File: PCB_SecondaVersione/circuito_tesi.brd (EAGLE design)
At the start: 100 x 80 mm, 52 parts, among them IC1 SCD41-D-R2, IC2 TPS60120PWPR, IC3 TPS78918DBVR, Q1 BSS138, Q2 BSS138, Q3 BSS138, Q4 BSS138, U1 TSV912IDT, U2 SGP30, U3 MICS-6814, U5 317030213, U6 BME280, U7 LIS3DH, U8 MAX682ESA+

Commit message: Sistemato circuito
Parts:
- removed C1, C12: CL05A106MP5NUNC, Condens_10uF:CAPC1005X55N
- removed C10, C11, C6: GRM033R60J105MEA2D, Condens_1uF:CAPC0603X35N
- removed C2, C3, C5: GRM033R61A225KE47D, Condens_2.2uF:CAPC0603X39N
- removed C4: CL05A226MQ5N6J8, Condens_22uF:CAPC1005X55N
- removed IC2: TPS60120PWPR, C_P_3.3_TPS60120PWPR:SOP65P640X120-21N
- removed IC3: TPS78918DBVR, V_REG_1.8_SOT-23-5:SOT95P280X145-5N
- removed R18: ERA6VEB8200V, Res_820_0p25W:RES_ERA6VEB8200V
- removed U8: MAX682ESA+, C_P_5_MAX682ESA_:SOIC127P600X175-8N
- added U10, U4, U9: LD1117S33TR, V_Reg_3.3_SMD:SOT230P700X180-4N
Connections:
- net N$15 renamed AIN3
- net N$17 renamed AIN1
- removed net 3.3: C13.1, C4.2, C5.2, IC2.16, Q3.1, Q4.1, R1.2, R11.2, R13.2, R14.2, R16.2, R18.2, R2.2, U5.11, U6.2, U6.6, U6.8, U7.1, U7.14, U7.8, U8.1, U8.3
- removed net N$14: C3.2, IC2.15
- removed net N$18: C3.1, IC2.13
- removed net N$19: IC2.4, IC2.5
- removed net N$20: C6.2, U8.6
- removed net N$22: C6.1, U8.7
- removed net N$23: Q1.2, R10.1, U2.6
- removed net N$24: R18.1, U8.2
- removed net N$7 (its old number): C2.2, IC2.6
- new net 3.3V: C13.1, IC1.19, IC1.7, Q3.1, Q4.1, R11.1, R13.2, R14.2, R16.1, U5.11, U6.2, U6.6, U6.8, U7.1, U7.14, U7.8, U9.2, U9.4
- new net N$25: BT3.-, BT4.S+1, BT4.S+2
- new net N$27: BT1.S+1, BT1.S+2, S2.2
- new net N$5: Q4.3, R17.1, SPS30.3
- new net SWDCLK: U5.36
- new net SWDIO: U5.37
- net 1.8V: now also R10.1, U10.2, U10.4; no longer C10.2, IC3.5, R10.2
- net 5V: now also U4.2, U4.4; no longer C12.1, IC1.19, IC1.7, U8.8
- net GND: now also U10.1, U4.1, U9.1; no longer BT3.-, C1.2, C10.1, C11.1, C12.2, C4.1, C5.1, IC2.1, IC2.10, IC2.11, IC2.12, IC2.19, IC2.2, IC2.20, IC2.9, IC3.2, U8.4, U8.5
- net N$1: no longer IC1.10
- net N$12: now also Q1.2, R10.2, U2.6; no longer C2.1, IC2.8
- net N$2: now also BT1.-; no longer BT1.S+1, BT1.S+2, S2.2
- net N$3: now also R1.1, R2.1; no longer IC1.9, Q4.3, R17.1, SPS30.3
- net N$4: no longer BT1.-, BT4.S+1, BT4.S+2
- net SCL: now also IC1.9, R1.2, R11.2, R16.2; no longer R11.1, R16.1, R2.1
- net SDA: now also IC1.10, R2.2; no longer R1.1
- net VDD: now also S2.1, U10.3, U4.3, U9.3; no longer C1.1, C11.2, IC2.14, IC2.3, IC2.7, IC3.1, IC3.3, S2.3
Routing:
- net 3.3: track 131.5 -> 0.00 mm, vias 6 -> 0
- net N$4: track 94.0 -> 0.00 mm
- net GND: track 77.9 -> 14.9 mm
- net 5V: track 60.9 -> 0.55 mm, vias 1 -> 0
- net N$2: track 60.0 -> 0.00 mm
- net SCL: track 58.6 -> 0.00 mm, vias 2 -> 0
- net SDA: track 64.2 -> 9.55 mm
- net 1.8V: track 45.5 -> 3.63 mm, vias 1 -> 0
- net 3.3V: track 0.00 -> 41.2 mm, vias 0 -> 1
- net VDD: track 40.0 -> 0.00 mm
- net N$23: track 10.3 -> 0.00 mm
- net N$3: track 8.36 -> 0.00 mm
- net AIN1: track 9.64 -> 2.09 mm
- net N$1: track 13.2 -> 9.63 mm
- net N$16: track 11.1 -> 7.86 mm
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
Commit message: Inizio PCB
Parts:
- moved C9 120.6 mm to (-81.3, 82.5), turned to 0 degrees
- moved LED2 117.3 mm to (-61.0, 14.0), turned to 0 degrees
- moved C7 114.7 mm to (-63.5, 82.5), turned to 0 degrees
- moved C8 110.9 mm to (-72.4, 82.5), turned to 0 degrees
- moved R1 110.1 mm to (-76.2, 72.4), turned to 0 degrees
- moved R17 101.2 mm to (-80.0, 78.7)
- moved R16 99.5 mm to (-72.4, 78.7)
- moved R9 99.0 mm to (-48.3, 82.5)
- moved C13 98.3 mm to (-54.6, 82.5), turned to 0 degrees
- moved U1 97.8 mm to (-73.7, 45.7)
- moved U6 94.6 mm to (-58.4, 72.4), turned to 0 degrees
- moved R8 88.1 mm to (-67.3, 72.4), turned to 0 degrees
- moved U2 86.4 mm to (-38.1, 73.7), turned to 0 degrees
- moved R12 86.3 mm to (-41.9, 78.7)
- moved U7 85.7 mm to (-53.3, 72.4), turned to 0 degrees
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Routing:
- net 3.3V: track 41.2 -> 0.00 mm, vias 1 -> 0
- net N$6: track 16.1 -> 0.00 mm
- net GND: track 14.9 -> 0.00 mm
- net N$21: track 9.71 -> 0.00 mm
- net N$1: track 9.63 -> 0.00 mm
- net SDA: track 9.55 -> 0.00 mm
- net N$16: track 7.86 -> 0.00 mm
- net AIN3: track 7.43 -> 0.00 mm
- net N$11: track 6.97 -> 0.00 mm
- net N$12: track 4.79 -> 0.00 mm
- net N$8: track 4.13 -> 0.00 mm
- net 1.8V: track 3.63 -> 0.00 mm
- net N$10: track 3.56 -> 0.00 mm
- net N$9: track 2.90 -> 0.00 mm
- net N$13: track 2.21 -> 0.00 mm
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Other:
- outline, holes or cut-outs redrawn
- board text removed: "QUA CONNETTORI SPS30"

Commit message: Aggiunto SGP30
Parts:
- removed S2: JS102011SAQN, switch_JS102011SAQN:SW_JS102011SAQN
- added S1: EG1213, switch_TH_HO:SW_EG1213
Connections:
- net N$27: now also S1.2; no longer S2.2
- net VDD: now also S1.1; no longer S2.1
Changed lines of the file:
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@@
 <attribute name="VALUE" x="-49.7" y="81.75" size="0.5" layer="27" align="top-left"/>
-</element>
-<element name="S2" library="switch_JS102011SAQN" package="SW_JS102011SAQN" value="JS102011SAQN" x="49.55" y="47.34" smashed="yes" rot="MR270">
-<attribute name="DESCRIPTION" value=" Slide Switch SPDT Surface Mount, Right Angle " x="94" y="-6" size="1.778" layer="28" rot="MR270" display="off"/>
-<attribute name="DIGI-KEY_PART_NUMBER" value="401-1999-2-ND" x="94" y="-6" size="1.778" layer="28" rot="MR270" display="off"/>
-<attribute name="MF" value="C&amp;K" x="94" y="-6" size="1.778" layer="28" rot="MR270" display="off"/>
-<attribute name="MP" value="JS102011SAQN" x="94" y="-6" size="1.778" layer="28" rot="MR270" display="off"/>
-<attribute name="NAME" x="52.5522" y="52.14353125" size="1.27093125" layer="26" rot="MR0"/>
-<attribute name="PACKAGE" value="None" x="94" y="-6" size="1.778" layer="28" rot="MR270" display="off"/>
-<attribute name="PURCHASE-URL" value="https://pricing.snapeda.com/search/part/JS102011SAQN/?ref=eda" x="94" y="-6" size="1.778" layer="28" rot="MR270" display="off"/>
-<attribute name="VALUE" x="52.85288125" y="41.23466875" size="1.271109375" layer="28" rot="MR0"/>
 </element>
 <element name="SPS30" library="con-lstb" library_urn="urn:adsk.eagle:library:162" package="MA05-1" package3d_urn="urn:adsk.eagle:package:8332/1" value="" x="-74.93" y="60.96" smashed="yes">
@@
 <attribute name="PURCHASE-URL" value="https://pricing.snapeda.com/search/part/LD1117S33TR/?ref=eda" x="0" y="0" size="1.778" layer="27" display="off"/>
 <attribute name="VALUE" x="-52.071190625" y="58.3668" size="1.270590625" layer="27"/>
+</element>
+<element name="S1" library="switch_TH_HO" package="SW_EG1213" value="EG1213" x="48.7" y="46.9" smashed="yes" rot="MR270">
+<attribute name="DESCRIPTION" value=" Slide Switch SPDT Through Hole, Right Angle " x="48.7" y="46.9" size="1.778" layer="28" rot="MR270" display="off"/>
+<attribute name="DIGI-KEY_PART_NUMBER" value="EG1906-ND" x="48.7" y="46.9" size="1.778" layer="28" rot="MR270" display="off"/>
+<attribute name="MF" value="E-Switch" x="48.7" y="46.9" size="1.778" layer="28" rot="MR270" display="off"/>
+<attribute name="MP" value="EG1213" x="48.7" y="46.9" size="1.778" layer="28" rot="MR270" display="off"/>
+<attribute name="PACKAGE" value="None" x="48.7" y="46.9" size="1.778" layer="28" rot="MR270" display="off"/>
+<attribute name="PURCHASE-URL" value="https://pricing.snapeda.com/search/part/EG1213/?ref=eda" x="48.7" y="46.9" size="1.778" layer="28" rot="MR270" display="off"/>
 </element>
 </elements>
@@
 <contactref element="BT1" pad="S+1"/>
 <contactref element="BT1" pad="S+2"/>
-<contactref element="S2" pad="2"/>
-<wire x1="32.84" y1="36.65" x2="47.44" y2="36.65" width="0" layer="19" extent="1-1"/>
-<wire x1="46.8" y1="47.34" x2="32.84" y2="36.65" width="0" layer="19" extent="1-1"/>
+<contactref element="S1" pad="2"/>
+<wire x1="32.84" y1="36.65" x2="48.7" y2="46.9" width="0" layer="19" extent="16-16"/>
+<wire x1="47.44" y1="36.65" x2="32.84" y2="36.65" width="0" layer="19" extent="16-16"/>
 </signal>
 <signal name="VDD">
-<contactref element="S2" pad="1"/>
 <contactref element="U4" pad="3"/>
 <contactref element="U9" pad="3"/>
 <contactref element="U10" pad="3"/>
-<wire x1="-52.43" y1="61.2" x2="-38.46" y2="61.2" width="0" layer="19" extent="1-1"/>
-<wire x1="-66.4" y1="61.2" x2="-52.43" y2="61.2" width="0" layer="19" extent="1-1"/>
-<wire x1="46.8" y1="49.84" x2="-52.43" y2="61.2" width="0" layer="19" extent="1-1"/>
+<contactref element="S1" pad="1"/>
+<wire x1="-66.4" y1="61.2" x2="48.7" y2="48.9" width="0" layer="19" extent="1-1"/>
+<wire x1="-52.43" y1="61.2" x2="-66.4" y2="61.2" width="0" layer="19" extent="1-1"/>
+<wire x1="-38.46" y1="61.2" x2="-52.43" y2="61.2" width="0" layer="19" extent="1-1"/>
 </signal>
 <signal name="3.3V">

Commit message: Aggiunto Voltage Regulators
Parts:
- removed U10, U4, U9: LD1117S33TR, V_Reg_3.3_SMD:SOT230P700X180-4N
- added C1, C2, C3, C4: GRM033C80J104KE15D, Condens_100nF:CAPC0603X33N
- added C5, C6: GRM033R60J105MEA2D, Condens_1uF:CAPC0603X35N
- added U11: MCP1711T-33I/OTSOT-23-5_OT_MCH, VOLT_REG_3.3_SOT-23-5:SOT-23-5_OT_MCH
- added U12, U8: MC78LC50NTRGTSOT23-5_ONS, VOLT_REG_5V_SOT-23-5:TSOT23-5_ONS
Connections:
- net 1.8V: now also C6.2, U12.5; no longer U10.2, U10.4
- net 3.3V: now also C2.2, U11.5; no longer U9.2, U9.4
- net 5V: now also C4.2, U8.3; no longer U4.2, U4.4
- net GND: now also C1.1, C2.1, C3.1, C4.1, C5.1, C6.1, U11.2, U12.2, U8.1; no longer U10.1, U4.1, U9.1
- net VDD: now also C1.2, C3.2, C5.2, U11.1, U11.3, U12.1, U12.3, U8.2; no longer U10.3, U4.3, U9.3

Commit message: Aggiunte capacità 0805
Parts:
- removed C1, C2, C3, C4, C7: GRM033C80J104KE15D, Condens_100nF:CAPC0603X33N
- removed C13: CL05A106MP5NUNC, Condens_10uF:CAPC1005X55N
- removed C5, C6: GRM033R60J105MEA2D, Condens_1uF:CAPC0603X35N
- removed C8, C9: GRM033R60J103KA01D, Condens_10nF:CAPC0603X33N
- removed LED2: SML-LX1206SRC-TRLED_3P2X1P5_LUM-L, LED_SMD:LED_3P2X1P5_LUM-L
- removed U11: MCP1711T-33I/OTSOT-23-5_OT_MCH, VOLT_REG_3.3_SOT-23-5:SOT-23-5_OT_MCH
- removed U12, U8: MC78LC50NTRGTSOT23-5_ONS, VOLT_REG_5V_SOT-23-5:TSOT23-5_ONS
- added C10_10: CL21A226MOQNNNE, Cond_22uF_0805:CAPC2012X135N
- added C1_0.1, C2_0.1, C7_0.01, C8_0.02, C9_0.1: CL21B104KCFNNNE, Cond_100nF_0805:CAPC2012X140N
- added C3_2.2, C4_470P: CL21A475KAQNNNE, Cond_4.7uF_0805:CAPC2012X140N
- added C5_1, C6_2: CL21B105KAFNNNE, Cond_1uF_0805:CAPC2012X140N
- added D1: LTST-C170TBKT, LED_0805:DIOC200X125X110
- added Q5: MMBT3904-215, BJT_TO-236:SOT95P230X110-3N
- added R29: RNCF0603DTE820R, Res_820OHM:RESC1508X55N
- added V_R_1.8: S-1318D18-M5T1U4, VOLT_REG_1.8_SOT-23-5:SOT95P275X130-5N
- added V_R_3.3: MIC5219-3.3YMMMSOP-8LD-PL-1_MCH, Volt_Reg_3.3_8MSOP:MSOP-8LD-PL-1_MCH
- added V_R_5: MC78LC50NTRGTSOT23-5_ONS, VOLT_REG_5V_SOT-23-5:TSOT23-5_ONS
- R11: value RNCP0805FTD10K0 -> RP73PF2A130RBTDF; device Res_10K_0p25W:RESC2012X60N -> Res_130_0p25:RESC2012X65N
- R12: value RNCP0805FTD10K0 -> ERA6VEB8200V; device Res_10K_0p25W:RESC2012X60N -> Res_820_0p25W:RES_ERA6VEB8200V
- R13, R14: value RNCP0805FTD10K0 -> RMCF0603FT5M10; device Res_10K_0p25W:RESC2012X60N -> Res_5.1MOHM:RESC1508X55N
- R15, R16: value RNCP0805FTD10K0 -> RMCF0603FT10M0; device Res_10K_0p25W:RESC2012X60N -> Res_10MOHM_2:RESC1508X55N
- R17: value RNCP0805FTD10K0 -> ERJ-PB6D5101V; device Res_10K_0p25W:RESC2012X60N -> Res_5.1K_0805:RESC2012X70N
- R3, R4: value RMCF0603FT10M0 -> RNCP0805FTD10K0; device Res_10MOHM_2:RESC1508X55N -> Res_10K_0p25W:RESC2012X60N
- R5, R6: value RMCF0603FT5M10 -> RNCP0805FTD10K0; device Res_5.1MOHM:RESC1508X55N -> Res_10K_0p25W:RESC2012X60N
- R7: value RP73PF2A130RBTDF -> RNCP0805FTD10K0; device Res_130_0p25:RESC2012X65N -> Res_10K_0p25W:RESC2012X60N
- R8: value ERA6VEB8200V -> RNCP0805FTD10K0; device Res_820_0p25W:RES_ERA6VEB8200V -> Res_10K_0p25W:RESC2012X60N
- R9: value RNCF0603DTE820R -> RNCP0805FTD10K0; device Res_820OHM:RESC1508X55N -> Res_10K_0p25W:RESC2012X60N
- moved R17 149.0 mm to (-88.0, -70.0)
- moved R16 47.1 mm to (-25.4, 82.5)
- moved R15 47.1 mm to (-17.8, 82.5)
- moved R7 32.4 mm to (-80.0, 78.7)
- moved R10 30.5 mm to (-57.1, 78.7)
- moved R12 26.2 mm to (-67.3, 72.4)
- moved R13 16.9 mm to (-33.0, 82.5)
- moved R14 16.9 mm to (-40.6, 82.5)
- moved R9 16.9 mm to (-64.8, 78.7)
- moved R11 15.3 mm to (-48.3, 72.4)
- moved R3 9.67 mm to (-26.7, 78.7)
- moved R4 9.67 mm to (-34.3, 78.7)
- moved R6 9.67 mm to (-49.5, 78.7)
- moved R5 9.67 mm to (-41.9, 78.7)
- moved R8 8.13 mm to (-72.4, 78.7)
- renumbered U1 to OPAMP
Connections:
- new net N$14: C4_470P.1, V_R_3.3.4
- new net N$15: Q5.1, R17.2
- net 1.8V: now also C6_2.1, C9_0.1.2, R3.1, R5.2, V_R_1.8.5; no longer C6.2, C7.1, R10.1, R12.2, U12.5
- net 3.3V: now also C10_10.2, C3_2.2.1, R10.2, R4.1, R6.2, R8.1, V_R_3.3.3; no longer C13.1, C2.2, R11.1, R13.2, R14.2, R16.1, U11.5
- net 5V: now also C2_0.1.1, R11.2, R12.2, R9.2, V_R_5.3; no longer C4.2, R15.2, R17.2, R8.2, U8.3
- net AIN1: now also C7_0.01.2, R13.2, R15.2; no longer C8.2, R3.2, R5.2
- net AIN3: now also C8_0.02.1, R14.1, R16.2; no longer C9.2, R4.2, R6.1
- net GND: now also C10_10.1, C1_0.1.2, C2_0.1.2, C3_2.2.2, C4_470P.2, C5_1.2, C6_2.2, C7_0.01.1, C8_0.02.2, C9_0.1.1, R15.1, R16.1, R29.1, V_R_1.8.2, V_R_3.3.5, V_R_3.3.6, V_R_3.3.7, V_R_3.3.8, V_R_5.1; no longer C1.1, C13.2, C2.1, C3.1, C4.1, C5.1, C6.1, C7.2, C8.1, C9.1, R3.1, R4.1, R9.1, U11.2, U12.2, U8.1
- net N$1: now also R9.1; no longer R15.1
- net N$11: now also R12.1; no longer R8.1
- net N$12: now also R3.2; no longer R10.2
- net N$13: now also R11.1; no longer R7.1
- net N$16: now also R5.1; no longer R12.1
- net N$21: now also D1.+; no longer LED2.2
- net N$5: now also R7.1; no longer R17.1
- net N$7: now also R14.2; no longer R6.2
- net N$8: now also R13.1; no longer R5.1
- net N$9: now also D1.-, R29.2; no longer LED2.1, R9.2
- net SCL: now also R4.2, R8.2; no longer R11.2, R16.2
- net SDA: now also R10.1, R6.1; no longer R13.1, R14.1
- net VDD: now also C1_0.1.1, C5_1.1, V_R_1.8.1, V_R_1.8.3, V_R_3.3.1, V_R_3.3.2, V_R_5.2; no longer C1.2, C3.2, C5.2, U11.1, U11.3, U12.1, U12.3, U8.2

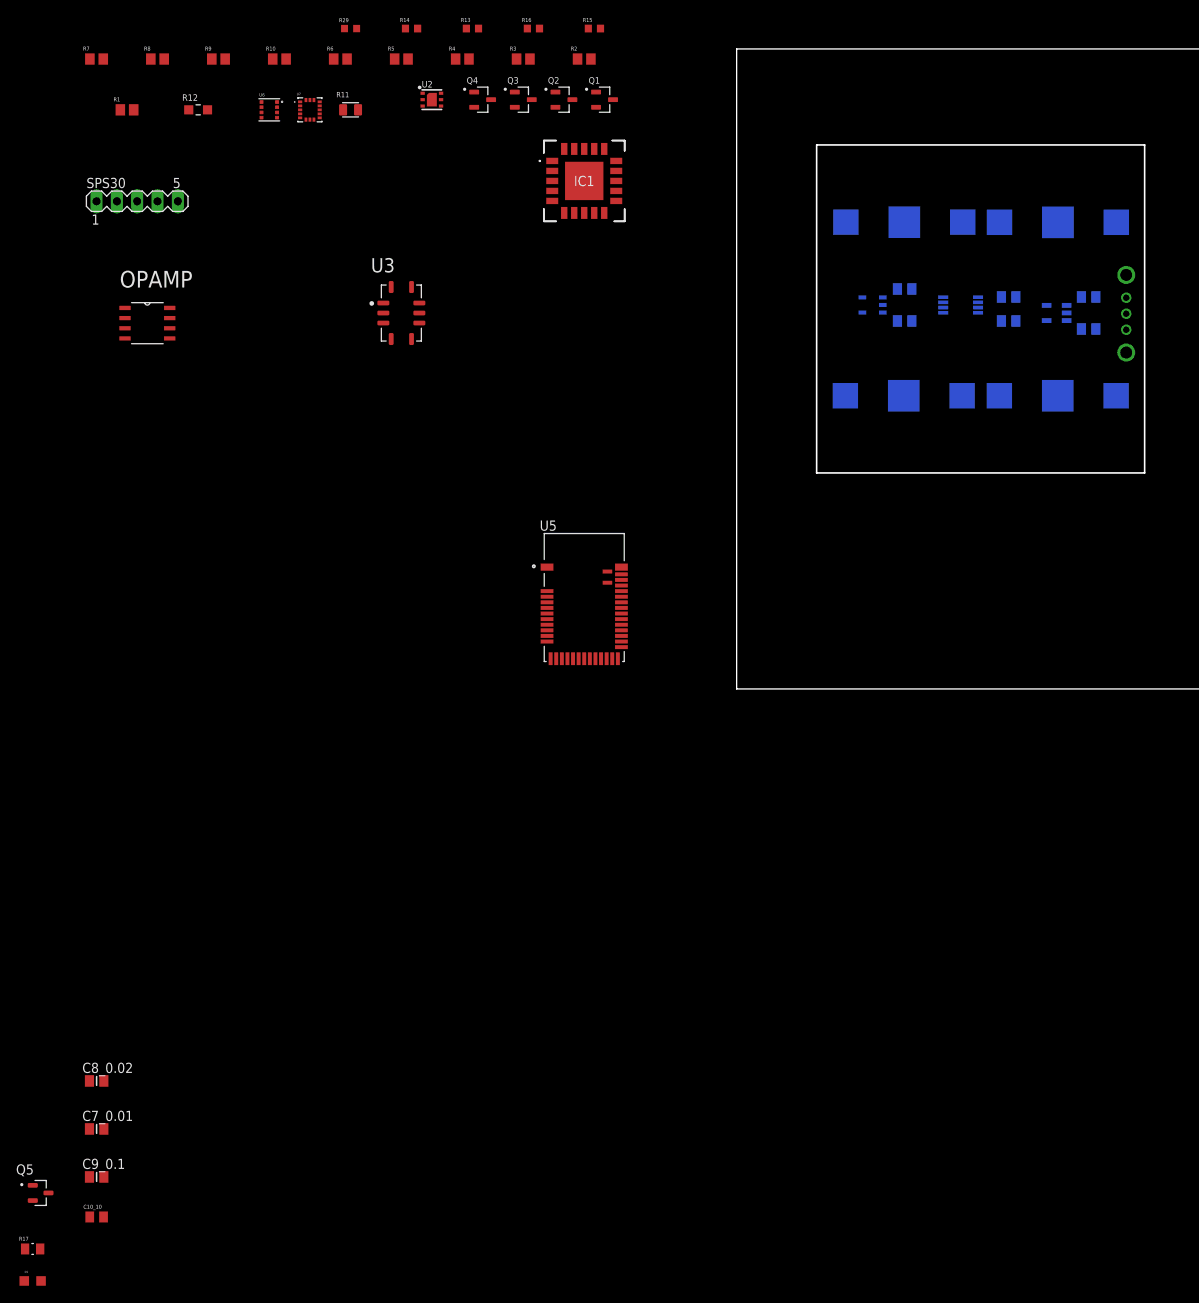
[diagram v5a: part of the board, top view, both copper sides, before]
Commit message: Sistemati nomi su Eagle
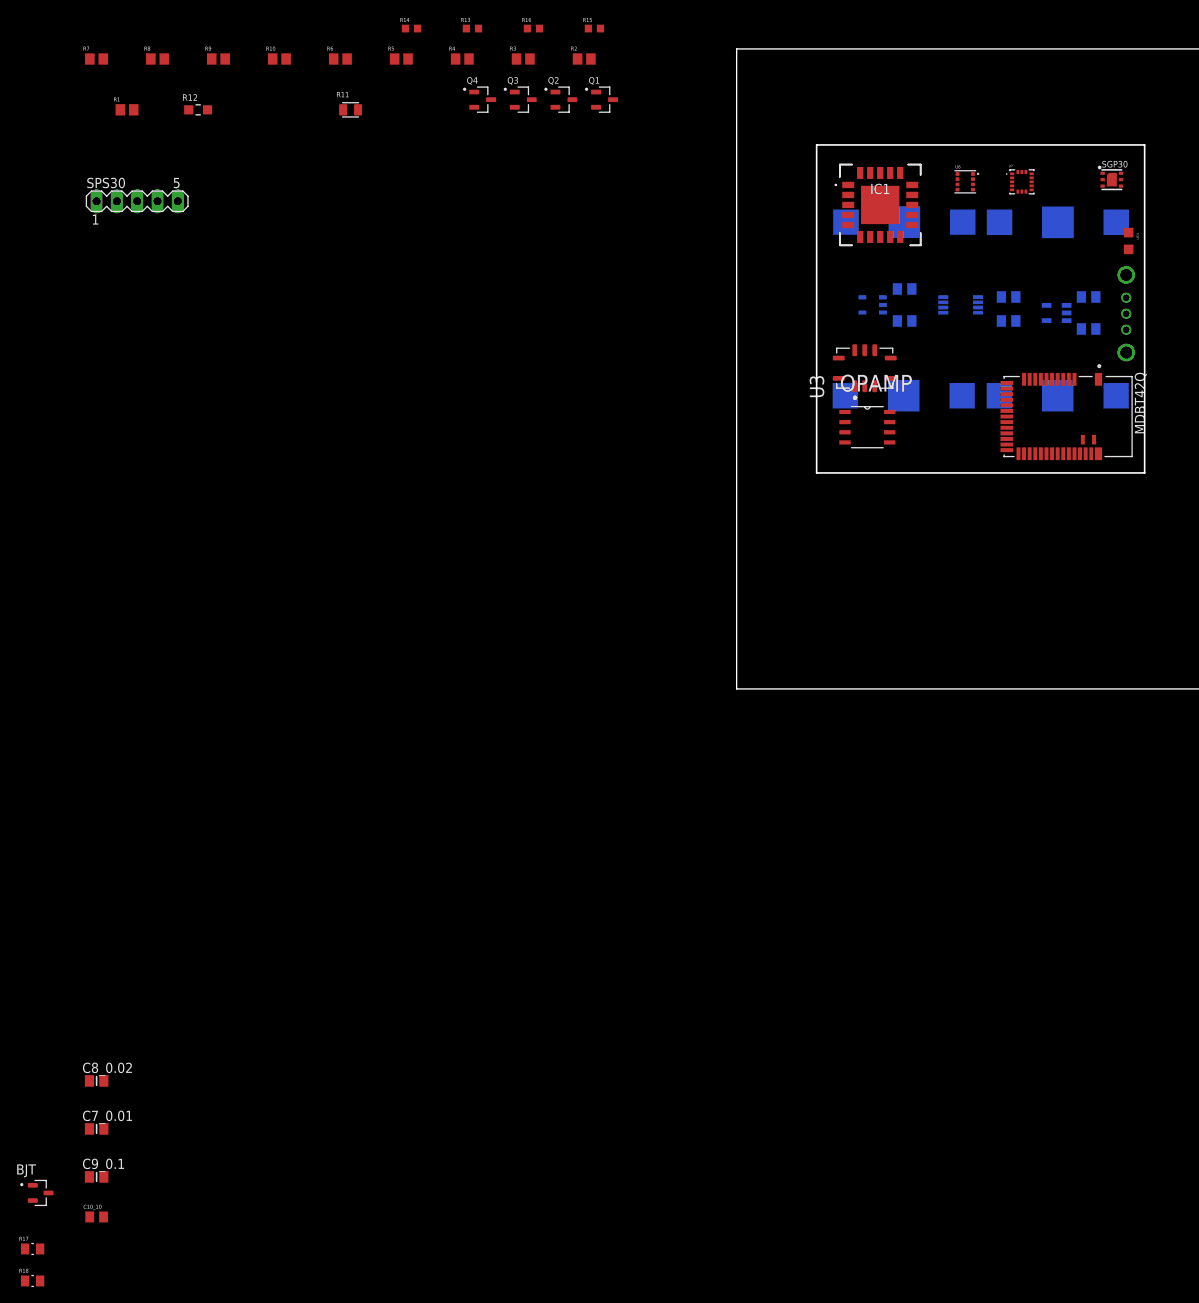
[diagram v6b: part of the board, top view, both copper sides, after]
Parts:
- removed D1: LTST-C170TBKT, LED_0805:DIOC200X125X110
- removed R29: RNCF0603DTE820R, Res_820OHM:RESC1508X55N
- removed U2: SGP30, SGP30:SGP30
- removed U5: 317030213, Raytac_nRF52:XCVR_317030213
- added LED1: LTST-C170TBKT, LED_0805:DIOC200X125X110
- added MDBT42Q: 317030213, Raytac_nRF52:XCVR_317030213
- added R18: ERJ-PB6B3300V, Res_330_0805:RESC2012X70N
- added SGP30: SGP30, SGP30:SGP30
- moved OPAMP 90.9 mm to (16.3, 32.7)
- moved U7 89.5 mm to (35.7, 63.4)
- moved U6 87.5 mm to (28.6, 63.4)
- moved U3 58.3 mm to (16.0, 40.1), turned to 90 degrees
- moved IC1 37.1 mm to (17.9, 60.5)
- renumbered Q5 to BJT
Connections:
- net 1.8V: now also SGP30.1, SGP30.5; no longer U2.1, U2.5
- net 3.3V: now also MDBT42Q.11; no longer U5.11
- net AIN1: now also MDBT42Q.16; no longer U5.16
- net AIN3: now also MDBT42Q.18; no longer U5.18
- net DCC: now also MDBT42Q.10; no longer U5.10
- net DEC4: now also MDBT42Q.9; no longer U5.9
- net GND: now also MDBT42Q.1, MDBT42Q.12, MDBT42Q.24, MDBT42Q.39, R18.1, SGP30.2, SGP30.4, SGP30.DIEPAD; no longer R29.1, U2.2, U2.4, U2.DIEPAD, U5.1, U5.12, U5.24, U5.39
- net N$12: now also SGP30.6; no longer U2.6
- net N$16: now also SGP30.3; no longer U2.3
- net N$21: now also LED1.+, MDBT42Q.2; no longer D1.+, U5.2
- net N$9: now also LED1.-, R18.2; no longer D1.-, R29.2
- net SCL: now also MDBT42Q.3; no longer U5.3
- net SDA: now also MDBT42Q.4; no longer U5.4
- net SWDCLK: now also MDBT42Q.36; no longer U5.36
- net SWDIO: now also MDBT42Q.37; no longer U5.37
